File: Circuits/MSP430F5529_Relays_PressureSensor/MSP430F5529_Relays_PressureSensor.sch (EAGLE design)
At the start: 10 parts, among them K1 AQV21SMD, K2 AQV21SMD, U2 SSCMRNN015PA3A3

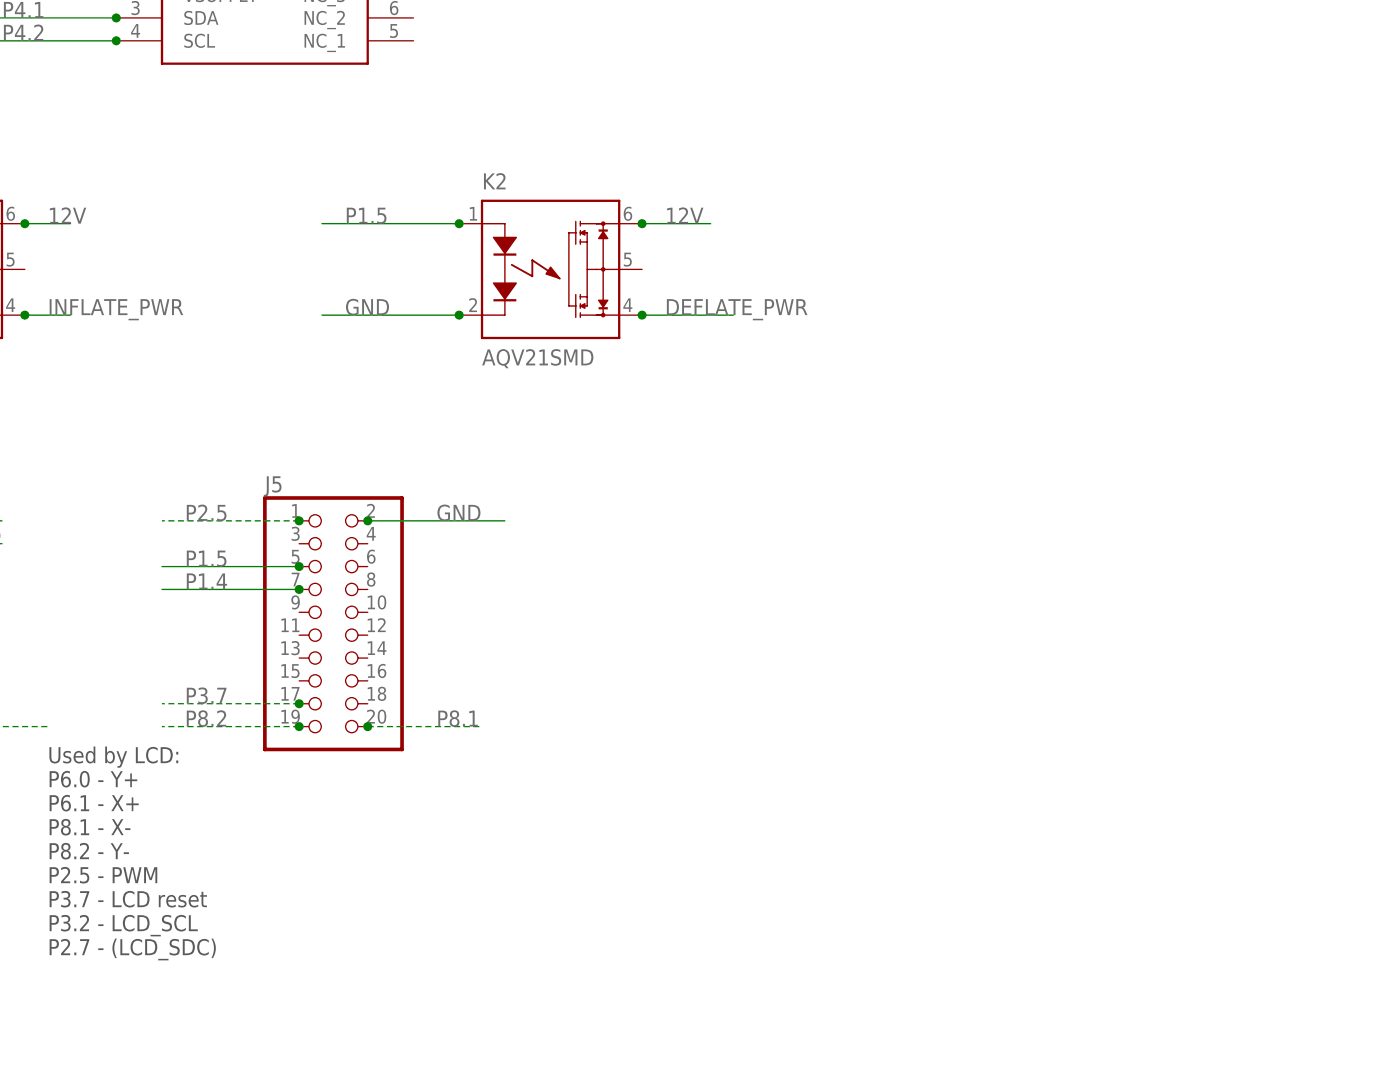
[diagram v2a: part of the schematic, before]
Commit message: Add switches for control of LCD instead of touchscreen
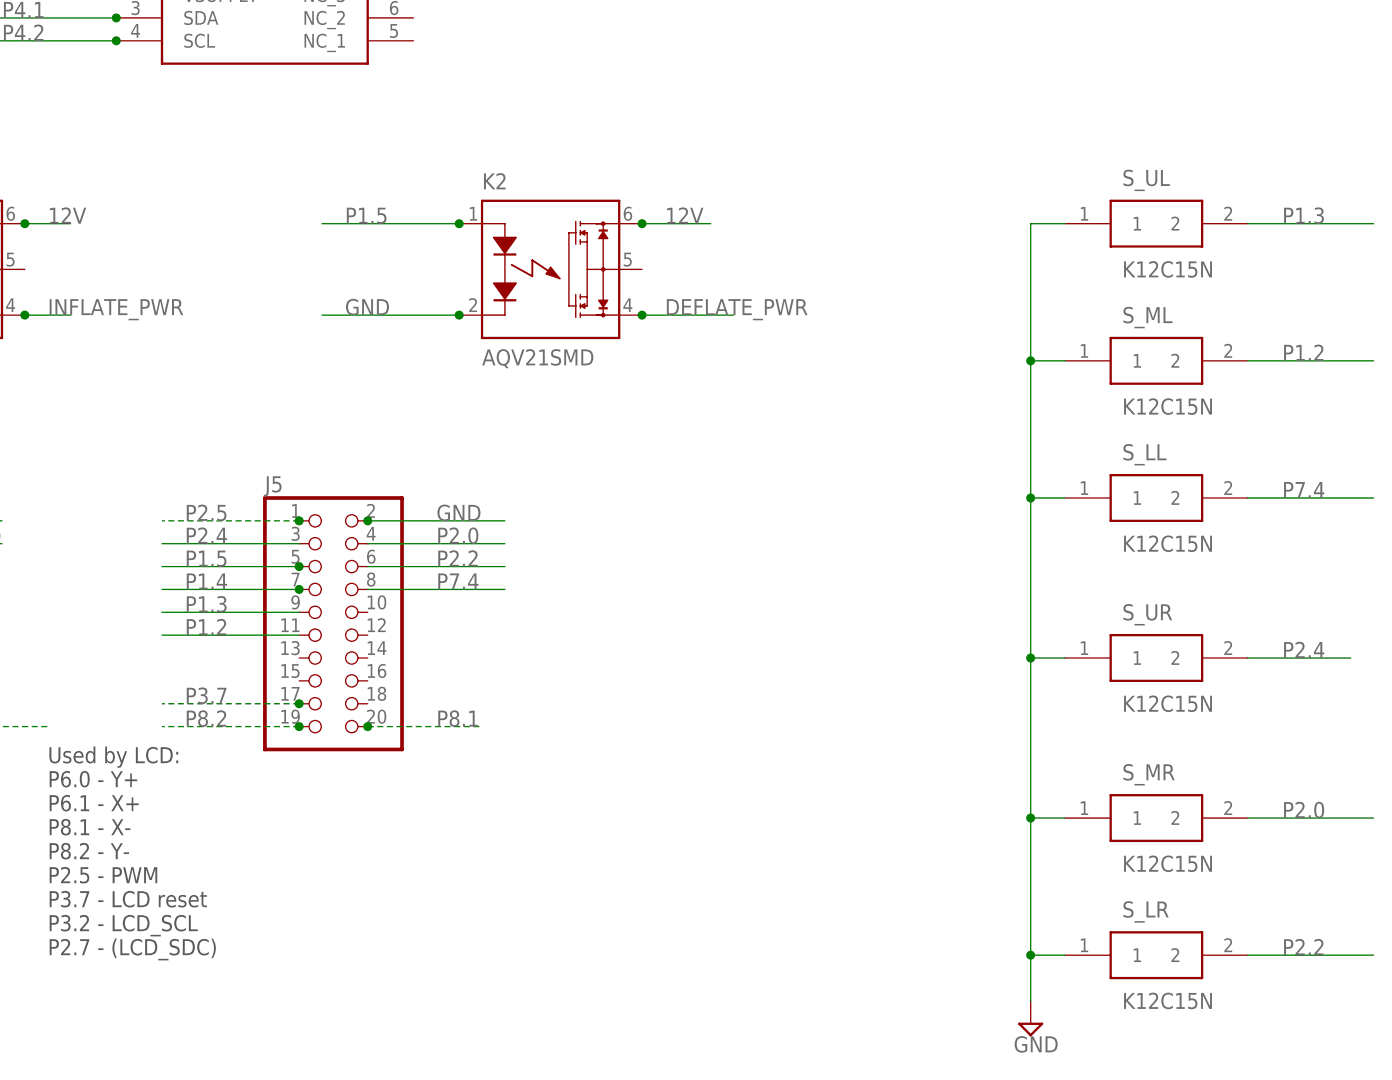
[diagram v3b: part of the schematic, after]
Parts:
- added S_LL, S_LR, S_ML, S_MR, S_UL, S_UR: K12C15N, SamacSys_Parts:K12C15N
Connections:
- new net P1.2: J5.11, S_ML.2
- new net P1.3: J5.9, S_UL.2
- new net P2.0: J5.4, S_MR.2
- new net P2.2: J5.6, S_LR.2
- new net P2.4: J5.3, S_UR.2
- new net P7.4: J5.8, S_LL.2
- net GND: now also S_LL.1, S_LR.1, S_ML.1, S_MR.1, S_UL.1, S_UR.1
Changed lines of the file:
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@@
 <part name="R2" library="resistor" library_urn="urn:adsk.eagle:library:348" deviceset="R-US_" device="M1206" package3d_urn="urn:adsk.eagle:package:26088/1" value="1k"/>
 <part name="U2" library="SamacSys_Parts" deviceset="SSCMRNN015PA3A3" device=""/>
+<part name="S_UL" library="SamacSys_Parts" deviceset="K12C15N" device=""/>
+<part name="S_ML" library="SamacSys_Parts" deviceset="K12C15N" device=""/>
+<part name="S_LL" library="SamacSys_Parts" deviceset="K12C15N" device=""/>
+<part name="S_UR" library="SamacSys_Parts" deviceset="K12C15N" device=""/>
+<part name="S_MR" library="SamacSys_Parts" deviceset="K12C15N" device=""/>
+<part name="S_LR" library="SamacSys_Parts" deviceset="K12C15N" device=""/>
+<part name="SUPPLY1" library="supply2" library_urn="urn:adsk.eagle:library:372" deviceset="GND" device=""/>
 </parts>
 <sheets>
@@
 <attribute name="VALUE" x="95.25" y="91.44" size="1.778" layer="96" align="center-left"/>
 </instance>
+<instance part="S_UL" gate="G$1" x="171.45" y="58.42" smashed="yes">
+<attribute name="NAME" x="177.8" y="63.5" size="1.778" layer="95" align="center-left"/>
+<attribute name="VALUE" x="177.8" y="53.34" size="1.778" layer="96" align="center-left"/>
+</instance>
+<instance part="S_ML" gate="G$1" x="171.45" y="43.18" smashed="yes">
+<attribute name="NAME" x="177.8" y="48.26" size="1.778" layer="95" align="center-left"/>
+<attribute name="VALUE" x="177.8" y="38.1" size="1.778" layer="96" align="center-left"/>
+</instance>
+<instance part="S_LL" gate="G$1" x="171.45" y="27.94" smashed="yes">
+<attribute name="NAME" x="177.8" y="33.02" size="1.778" layer="95" align="center-left"/>
+<attribute name="VALUE" x="177.8" y="22.86" size="1.778" layer="96" align="center-left"/>
+</instance>
+<instance part="S_UR" gate="G$1" x="171.45" y="10.16" smashed="yes">
+<attribute name="NAME" x="177.8" y="15.24" size="1.778" layer="95" align="center-left"/>
+<attribute name="VALUE" x="177.8" y="5.08" size="1.778" layer="96" align="center-left"/>
+</instance>
+<instance part="S_MR" gate="G$1" x="171.45" y="-7.62" smashed="yes">
+<attribute name="NAME" x="177.8" y="-2.54" size="1.778" layer="95" align="center-left"/>
+<attribute name="VALUE" x="177.8" y="-12.7" size="1.778" layer="96" align="center-left"/>
+</instance>
+<instance part="S_LR" gate="G$1" x="171.45" y="-22.86" smashed="yes">
+<attribute name="NAME" x="177.8" y="-17.78" size="1.778" layer="95" align="center-left"/>
+<attribute name="VALUE" x="177.8" y="-27.94" size="1.778" layer="96" align="center-left"/>
+</instance>
+<instance part="SUPPLY1" gate="GND" x="167.64" y="-30.48" smashed="yes">
+<attribute name="VALUE" x="165.735" y="-33.655" size="1.778" layer="96"/>
+</instance>
 </instances>
 <busses>
@@
 <junction x="0" y="43.18"/>
 </segment>
+<segment>
+<pinref part="SUPPLY1" gate="GND" pin="GND"/>
+<pinref part="S_LR" gate="G$1" pin="1"/>
+<wire x1="167.64" y1="58.42" x2="167.64" y2="43.18" width="0.1524" layer="91"/>
+<wire x1="167.64" y1="43.18" x2="167.64" y2="27.94" width="0.1524" layer="91"/>
+<wire x1="167.64" y1="27.94" x2="167.64" y2="10.16" width="0.1524" layer="91"/>
+<wire x1="167.64" y1="10.16" x2="167.64" y2="-7.62" width="0.1524" layer="91"/>
+<wire x1="167.64" y1="-7.62" x2="167.64" y2="-22.86" width="0.1524" layer="91"/>
+<wire x1="167.64" y1="-22.86" x2="167.64" y2="-27.94" width="0.1524" layer="91"/>
+<wire x1="171.45" y1="-22.86" x2="167.64" y2="-22.86" width="0.1524" layer="91"/>
+<junction x="167.64" y="-22.86"/>
+<pinref part="S_MR" gate="G$1" pin="1"/>
+<wire x1="171.45" y1="-7.62" x2="167.64" y2="-7.62" width="0.1524" layer="91"/>
+<junction x="167.64" y="-7.62"/>
+<pinref part="S_UR" gate="G$1" pin="1"/>
+<wire x1="171.45" y1="10.16" x2="167.64" y2="10.16" width="0.1524" layer="91"/>
+<junction x="167.64" y="10.16"/>
+<pinref part="S_LL" gate="G$1" pin="1"/>
+<wire x1="171.45" y1="27.94" x2="167.64" y2="27.94" width="0.1524" layer="91"/>
+<junction x="167.64" y="27.94"/>
+<pinref part="S_ML" gate="G$1" pin="1"/>
+<wire x1="171.45" y1="43.18" x2="167.64" y2="43.18" width="0.1524" layer="91"/>
+<junction x="167.64" y="43.18"/>
+<pinref part="S_UL" gate="G$1" pin="1"/>
+<wire x1="171.45" y1="58.42" x2="167.64" y2="58.42" width="0.1524" layer="91"/>
+</segment>
 </net>
 <net name="P4.1" class="0">
@@
 </segment>
 </net>
+<net name="P2.0" class="0">
+<segment>
+<pinref part="J5" gate="A" pin="4"/>
+<wire x1="93.98" y1="22.86" x2="109.22" y2="22.86" width="0.1524" layer="91"/>
+<label x="101.6" y="22.86" size="1.778" layer="95"/>
+</segment>
+<segment>
+<pinref part="S_MR" gate="G$1" pin="2"/>
+<wire x1="191.77" y1="-7.62" x2="205.74" y2="-7.62" width="0.1524" layer="91"/>
+<label x="195.58" y="-7.62" size="1.778" layer="95"/>
+</segment>
+</net>
+<net name="P2.2" class="0">
+<segment>
+<pinref part="J5" gate="A" pin="6"/>
+<wire x1="93.98" y1="20.32" x2="109.22" y2="20.32" width="0.1524" layer="91"/>
+<label x="101.6" y="20.32" size="1.778" layer="95"/>
+</segment>
+<segment>
+<pinref part="S_LR" gate="G$1" pin="2"/>
+<wire x1="191.77" y1="-22.86" x2="205.74" y2="-22.86" width="0.1524" layer="91"/>
+<label x="195.58" y="-22.86" size="1.778" layer="95"/>
+</segment>
+</net>
+<net name="P2.4" class="0">
+<segment>
+<pinref part="J5" gate="A" pin="3"/>
+<wire x1="86.36" y1="22.86" x2="71.12" y2="22.86" width="0.1524" layer="91"/>
+<label x="73.66" y="22.86" size="1.778" layer="95"/>
+</segment>
+<segment>
+<pinref part="S_UR" gate="G$1" pin="2"/>
+<wire x1="191.77" y1="10.16" x2="203.2" y2="10.16" width="0.1524" layer="91"/>
+<label x="195.58" y="10.16" size="1.778" layer="95"/>
+</segment>
+</net>
+<net name="P7.4" class="0">
+<segment>
+<pinref part="J5" gate="A" pin="8"/>
+<wire x1="93.98" y1="17.78" x2="109.22" y2="17.78" width="0.1524" layer="91"/>
+<label x="101.6" y="17.78" size="1.778" layer="95"/>
+</segment>
+<segment>
+<pinref part="S_LL" gate="G$1" pin="2"/>
+<wire x1="191.77" y1="27.94" x2="205.74" y2="27.94" width="0.1524" layer="91"/>
+<label x="195.58" y="27.94" size="1.778" layer="95"/>
+</segment>
+</net>
+<net name="P1.2" class="0">
+<segment>
+<pinref part="J5" gate="A" pin="11"/>
+<wire x1="86.36" y1="12.7" x2="71.12" y2="12.7" width="0.1524" layer="91"/>
+<label x="73.66" y="12.7" size="1.778" layer="95"/>
+</segment>
+<segment>
+<pinref part="S_ML" gate="G$1" pin="2"/>
+<wire x1="191.77" y1="43.18" x2="205.74" y2="43.18" width="0.1524" layer="91"/>
+<label x="195.58" y="43.18" size="1.778" layer="95"/>
+</segment>
+</net>
+<net name="P1.3" class="0">
+<segment>
+<pinref part="J5" gate="A" pin="9"/>
+<wire x1="86.36" y1="15.24" x2="76.2" y2="15.24" width="0.1524" layer="91"/>
+<wire x1="76.2" y1="15.24" x2="73.66" y2="15.24" width="0.1524" layer="91"/>
+<wire x1="73.66" y1="15.24" x2="71.12" y2="15.24" width="0.1524" layer="91"/>
+<label x="73.66" y="15.24" size="1.778" layer="95"/>
+</segment>
+<segment>
+<pinref part="S_UL" gate="G$1" pin="2"/>
+<wire x1="191.77" y1="58.42" x2="205.74" y2="58.42" width="0.1524" layer="91"/>
+<label x="195.58" y="58.42" size="1.778" layer="95"/>
+</segment>
+</net>

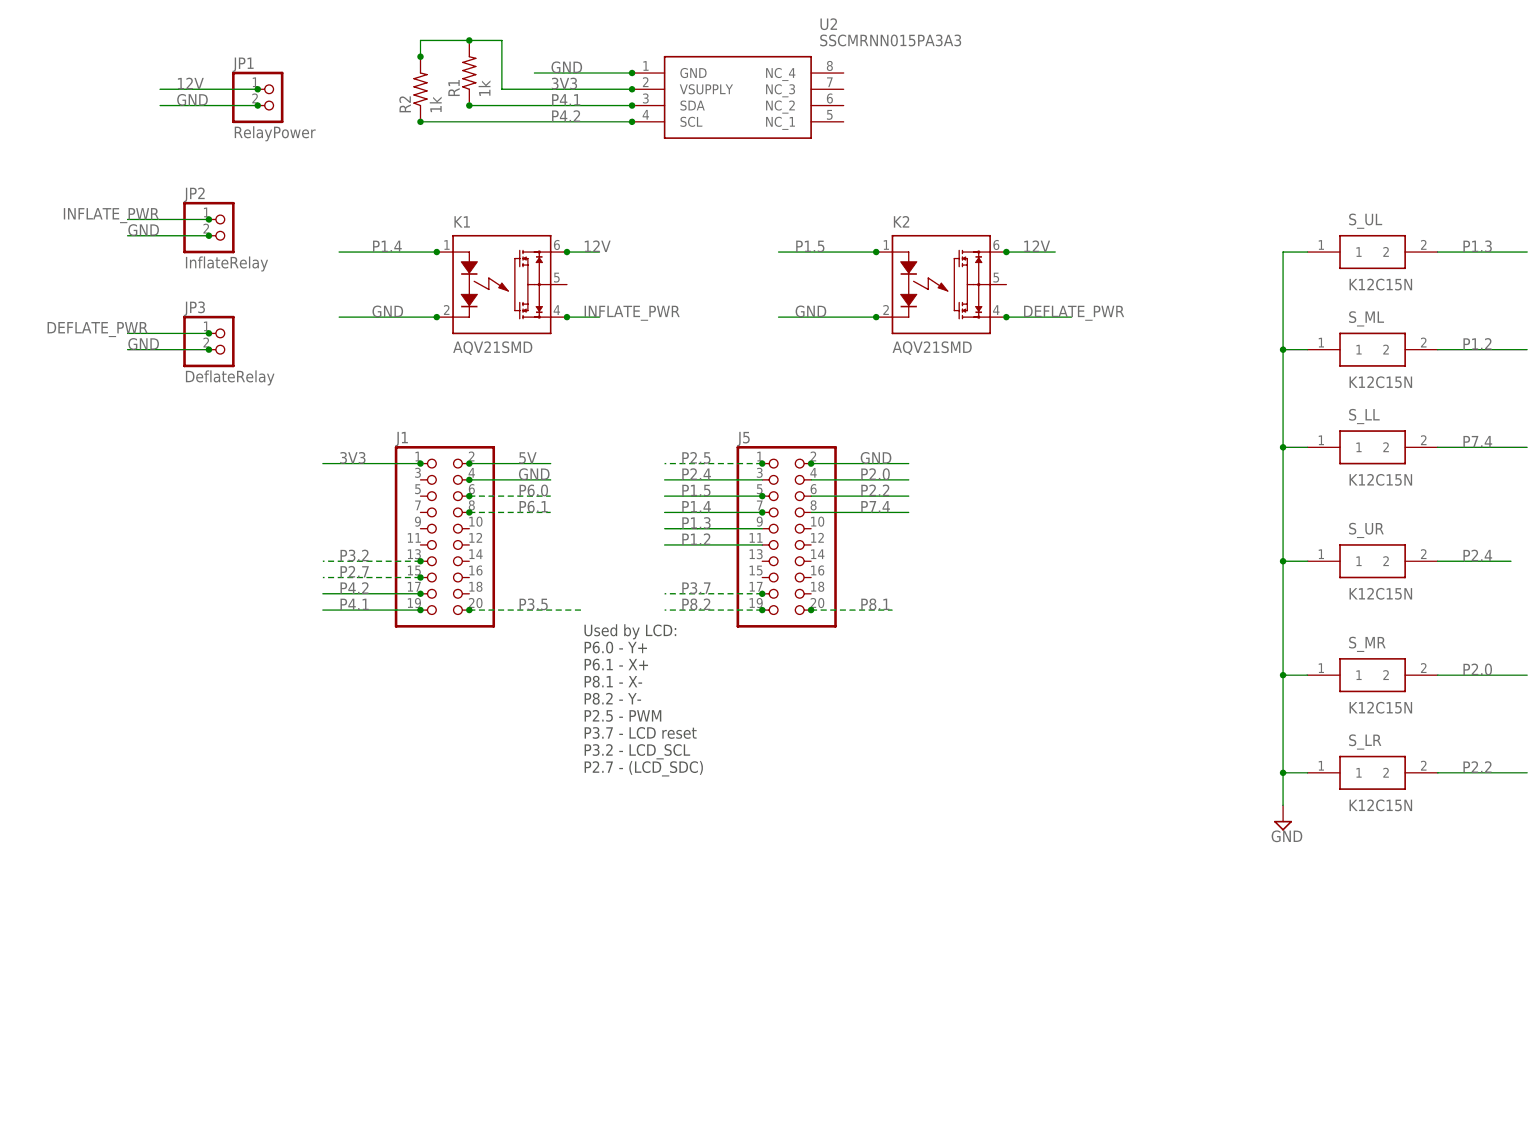
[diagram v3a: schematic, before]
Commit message: Add power supply and connector for GUI_Switches board
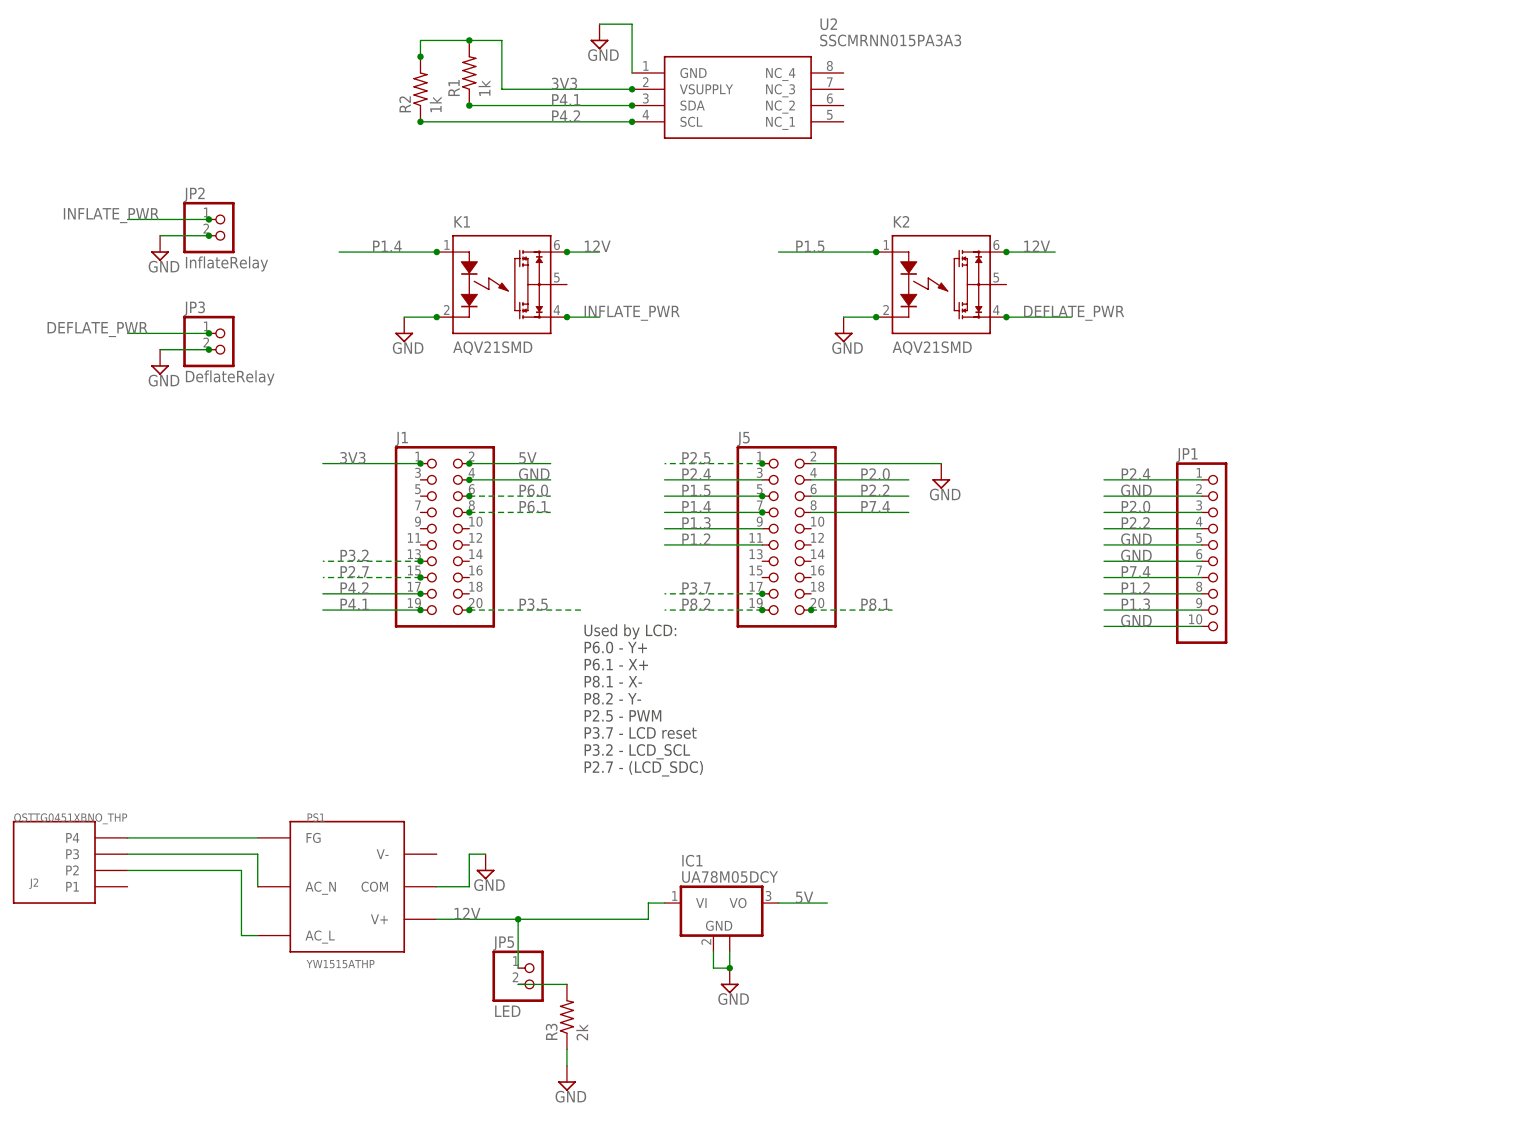
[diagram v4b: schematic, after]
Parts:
- removed S_LL, S_LR, S_ML, S_MR, S_UL, S_UR: K12C15N, SamacSys_Parts:K12C15N
- added IC1: UA78M05DCY, linear:UA78M05DCY
- added J2: OSTTG0451XBNO_THP, MasterSPIS:OSTTG0451XBNO_THP
- added JP5: LED, pinhead:PINHD-1X2/90
- added PS1: YW1515ATHP, MasterSPIS:YW1515ATHP
- added R3: 2k, resistor:R-US_M1206
- JP1: value RelayPower -> (none); device pinhead:PINHD-1X2/90 -> pinhead:PINHD-1X10/90
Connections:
- new net AC_L: J2.P2, PS1.AC_L
- new net AC_N: J2.P3, PS1.AC_N
- new net FG: J2.P4, PS1.FG
- new net N$1: JP5.2, R3.2
- net 12V: now also IC1.VI, JP5.1, PS1.V+; no longer JP1.1
- net 5V: now also IC1.VO
- net GND: now also IC1.GND, IC1.GND@1, JP1.10, JP1.5, JP1.6, PS1.COM, R3.1; no longer S_LL.1, S_LR.1, S_ML.1, S_MR.1, S_UL.1, S_UR.1
- net P1.2: now also JP1.8; no longer S_ML.2
- net P1.3: now also JP1.9; no longer S_UL.2
- net P2.0: now also JP1.3; no longer S_MR.2
- net P2.2: now also JP1.4; no longer S_LR.2
- net P2.4: now also JP1.1; no longer S_UR.2
- net P7.4: now also JP1.7; no longer S_LL.2

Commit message: Fix mistakes where power supply and terminal on bottom but use bottom traces Put both on top (top of supply will still be below LCD) and fix traces Some other minor layout adjustments (move pressure sensor closer to jumper, no reason for it to be near edge)
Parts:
- JP1: value (none) -> SWITCHES
- PS1: value YW1515ATHP -> YW1515ANO_THP; device MasterSPIS:YW1515ATHP -> MasterSPIS:YW1515ANO_THP
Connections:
- net AC_L: now also J2.P3; no longer J2.P2
- net AC_N: now also J2.P2; no longer J2.P3
- net FG: now also J2.P1; no longer J2.P4
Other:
- moved on the sheet: J2
